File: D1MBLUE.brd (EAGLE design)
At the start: 25.4 x 33 mm, 7 parts, among them U1 HC_05

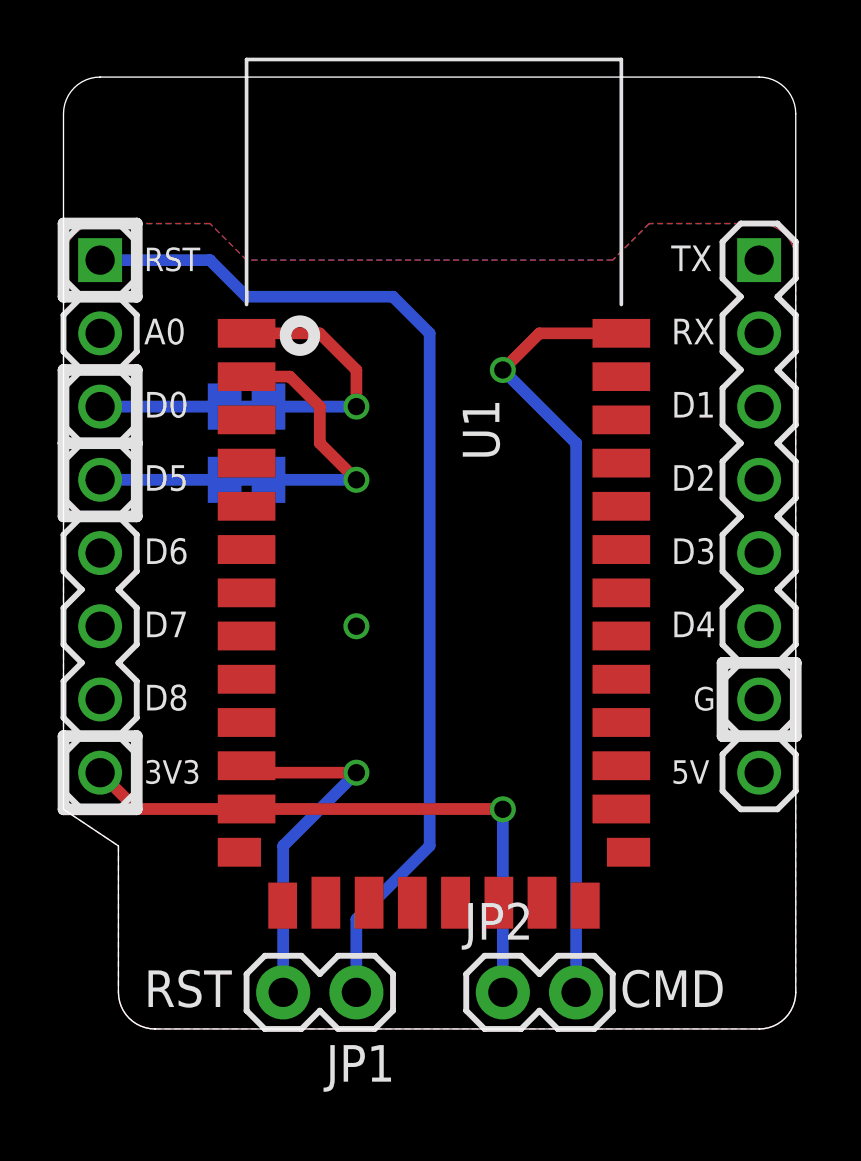
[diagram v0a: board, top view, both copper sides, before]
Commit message: Improved silkscreen and updated preview images
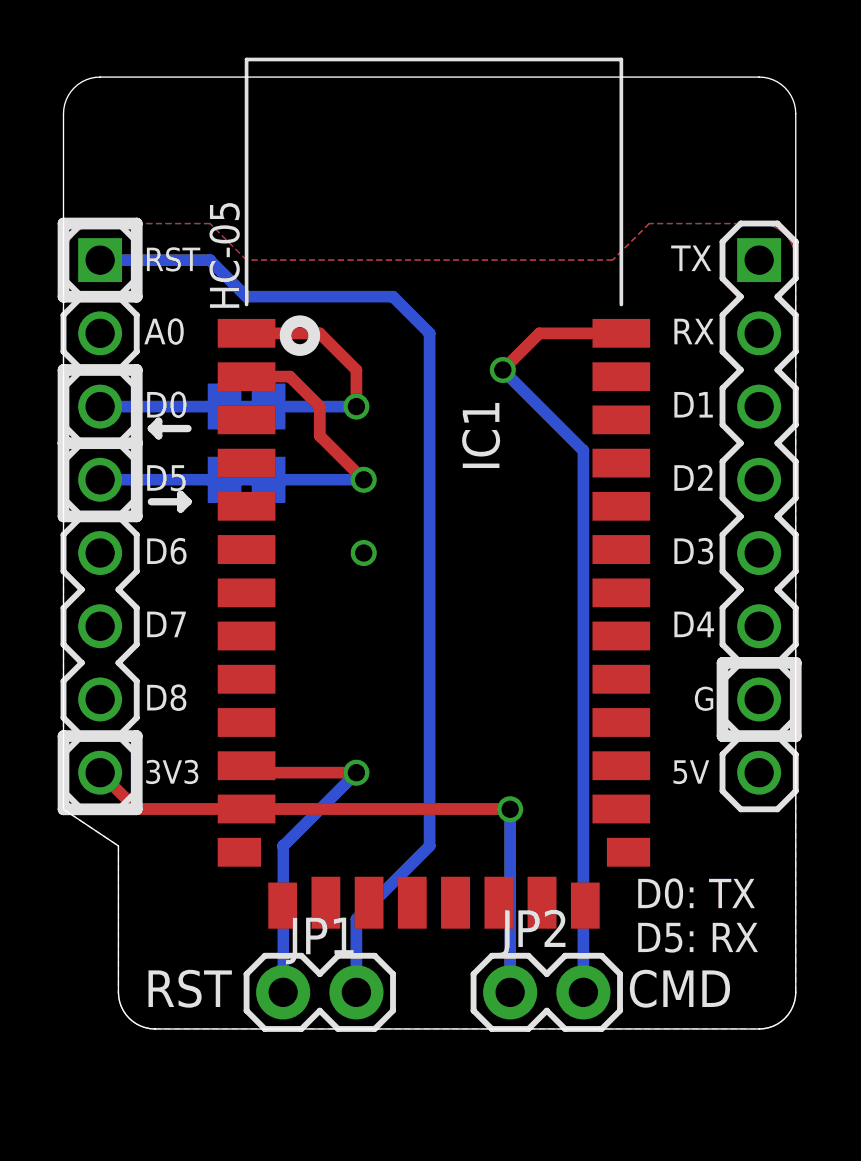
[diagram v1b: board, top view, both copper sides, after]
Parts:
- moved JP2 0.25 mm to (15.5, 1.27)
- renumbered U$2 to SJ1, U$3 to SJ2, U1 to IC1
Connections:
- net N$2 renamed BT-TX
- net N$4 renamed BT-RX
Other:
- board text added: "(C)2016 SuperHouse Automation Pty Ltd"
- board text added: "BT RX"
- board text added: "BT TX"
- board text added: "Bluetooth Serial Shield for D1 Mini"
- board text added: "D0: TX D5: RX"
- board text added: "GND"
- board text added: "HC-05"
- board text added: "SKU: D1MBLUE"
- board text added: "by Jon Oxer"
- board text added: "superhouse.tv/d1mblue"
- board text added: "v1.0"
